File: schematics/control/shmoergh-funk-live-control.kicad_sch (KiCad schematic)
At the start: 9 parts

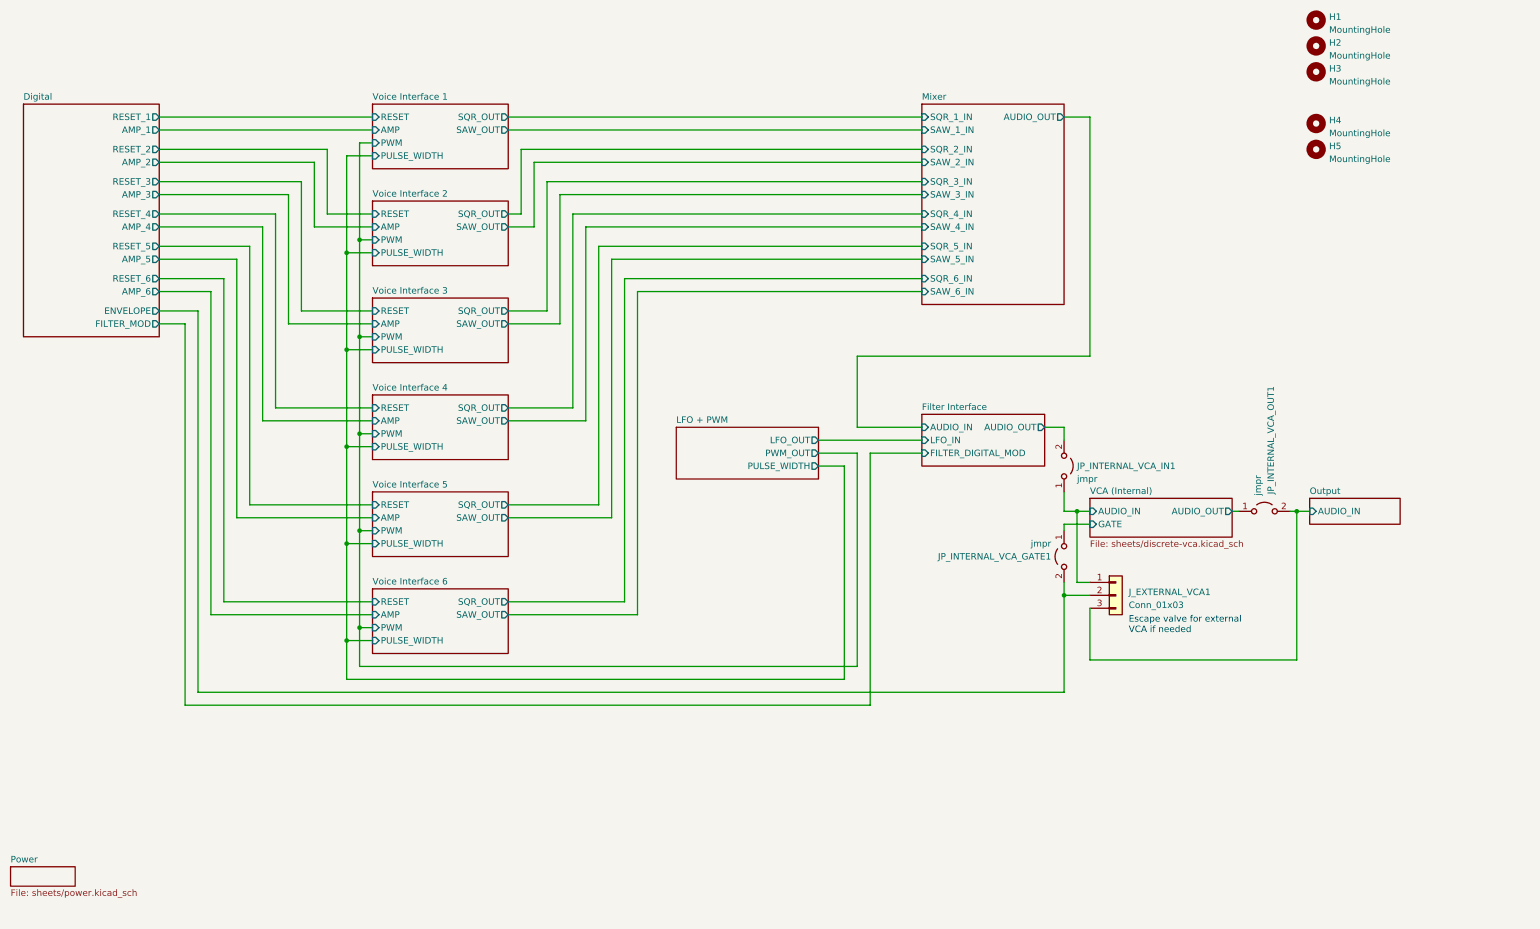
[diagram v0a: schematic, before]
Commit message: Added all UI components to schematics
- digital UI
- filter UI
- updated voice interface connection
- simplified schematics a lot
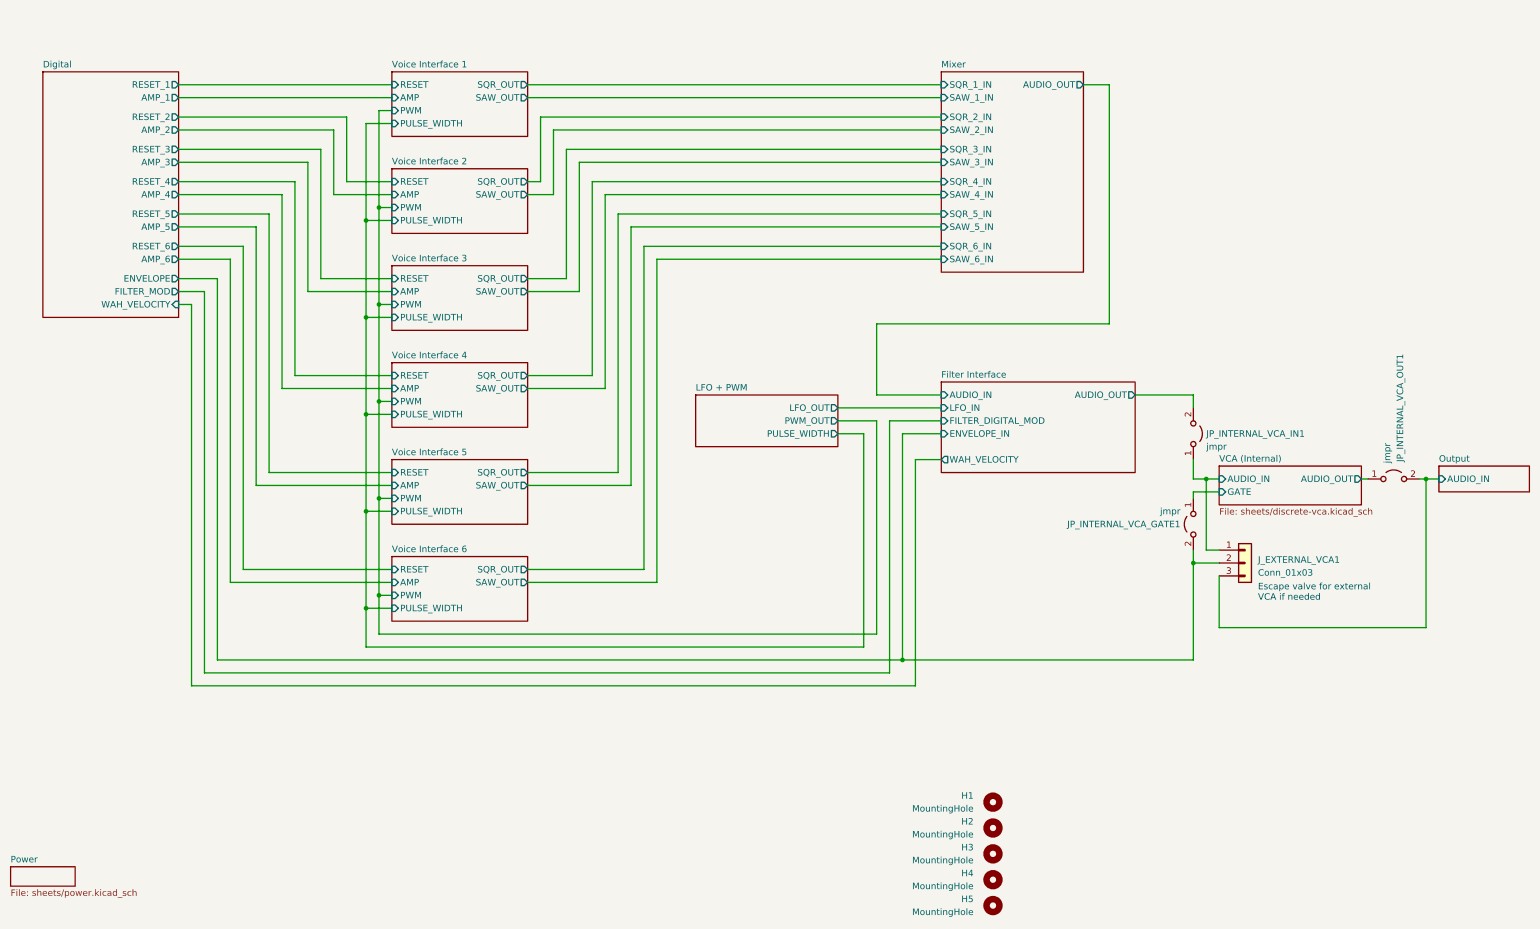
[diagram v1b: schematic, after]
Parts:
- H1, H2, H3, H4, H5: footprint MountingHole:MountingHole_3mm_Pad -> (none)
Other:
- sheet Digital ports: added WAH_VELOCITY; removed none
- sheet Filter Interface ports: added ENVELOPE_IN, WAH_VELOCITY; removed none
- moved on the sheet: H1, H2, H3, H4, H5, JP_INTERNAL_VCA_GATE1, JP_INTERNAL_VCA_IN1, JP_INTERNAL_VCA_OUT1, J_EXTERNAL_VCA1

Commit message: Schemo work
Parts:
- H1, H2, H3, H4, H5: footprint (none) -> MountingHole:MountingHole_3mm_Pad
- JP_INTERNAL_VCA_GATE1, JP_INTERNAL_VCA_IN1, JP_INTERNAL_VCA_OUT1: footprint (none) -> PCM_Jumper_AKL_Double:Jumper_P2.54mm_D0.7mm
- J_EXTERNAL_VCA1: footprint (none) -> Shmoergh_Custom_Footprints:NSL25_01x03_Vertical
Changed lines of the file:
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@@
       (effects (font (size 1.27 1.27)) (justify right))
     )
-    (property "Footprint" "" (at 213.36 191.77 0)
+    (property "Footprint" "MountingHole:MountingHole_3mm_Pad" (at 213.36 191.77 0)
       (effects (font (size 1.27 1.27)) hide)
     )
@@
       (effects (font (size 1.27 1.27)) (justify left))
     )
-    (property "Footprint" "" (at 252.73 99.06 0)
+    (property "Footprint" "PCM_Jumper_AKL_Double:Jumper_P2.54mm_D0.7mm" (at 252.73 99.06 0)
       (effects (font (size 1.27 1.27)) hide)
     )
@@
       (effects (font (size 1.27 1.27)) (justify left))
     )
-    (property "Footprint" "" (at 252.73 116.84 0)
+    (property "Footprint" "PCM_Jumper_AKL_Double:Jumper_P2.54mm_D0.7mm" (at 252.73 116.84 0)
       (effects (font (size 1.27 1.27)) hide)
     )
@@
       (effects (font (size 1.27 1.27)) (justify right))
     )
-    (property "Footprint" "" (at 213.36 186.69 0)
+    (property "Footprint" "MountingHole:MountingHole_3mm_Pad" (at 213.36 186.69 0)
       (effects (font (size 1.27 1.27)) hide)
     )
@@
       (effects (font (size 1.27 1.27)))
     )
-    (property "Footprint" "" (at 292.1 107.95 0)
+    (property "Footprint" "PCM_Jumper_AKL_Double:Jumper_P2.54mm_D0.7mm" (at 292.1 107.95 0)
       (effects (font (size 1.27 1.27)) hide)
     )
@@
       (effects (font (size 1.27 1.27)) (justify right))
     )
-    (property "Footprint" "" (at 213.36 181.61 0)
+    (property "Footprint" "MountingHole:MountingHole_3mm_Pad" (at 213.36 181.61 0)
       (effects (font (size 1.27 1.27)) hide)
     )
@@
       (effects (font (size 1.27 1.27)) (justify left))
     )
-    (property "Footprint" "" (at 262.89 124.46 0)
+    (property "Footprint" "Shmoergh_Custom_Footprints:NSL25_01x03_Vertical" (at 262.89 124.46 0)
       (effects (font (size 1.27 1.27)) hide)
     )
@@
       (effects (font (size 1.27 1.27)) (justify right))
     )
-    (property "Footprint" "" (at 213.36 171.45 0)
+    (property "Footprint" "MountingHole:MountingHole_3mm_Pad" (at 213.36 171.45 0)
       (effects (font (size 1.27 1.27)) hide)
     )
@@
       (effects (font (size 1.27 1.27)) (justify right))
     )
-    (property "Footprint" "" (at 213.36 176.53 0)
+    (property "Footprint" "MountingHole:MountingHole_3mm_Pad" (at 213.36 176.53 0)
       (effects (font (size 1.27 1.27)) hide)
     )
